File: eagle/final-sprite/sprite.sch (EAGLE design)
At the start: 62 parts, among them P1 SPRITE_PIN, P2 SPRITE_PIN, U1 CC430F5137, U2 DRV8833CRTER, U3 DRV8833CRTER, X1 TCXO_7Z

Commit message: Add review comments
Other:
- note added: "16 V"
- note added: "Eliminate pull-up"
- note added: "No interrupts? What's Data ENable?"
- note added: "Not connected... remove?"
- note added: "Regulated voltage output 1.5 (see Table 7)"
- note added: "Top row connectivity seems incorrect... Should be voltage dividers"
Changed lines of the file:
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@@
 <text x="-12.7" y="-264.16" size="1.778" layer="91">FIRMWARE:
 Pull-up required on NFAULT</text>
+<text x="182.88" y="-78.74" size="1.778" layer="91">Regulated voltage output 1.5
+(see Table 7)</text>
+<text x="182.88" y="-142.24" size="1.778" layer="91">Top row connectivity seems incorrect...
+Should be voltage dividers</text>
+<text x="91.44" y="-132.08" size="1.778" layer="91">Not connected... remove?</text>
+<text x="-17.78" y="-104.14" size="1.778" layer="91">16 V</text>
+<text x="48.26" y="-88.9" size="1.778" layer="91">Eliminate pull-up</text>
+<text x="27.94" y="-116.84" size="1.778" layer="91">No interrupts?
+What's Data ENable?</text>
 </plain>
 <instances>

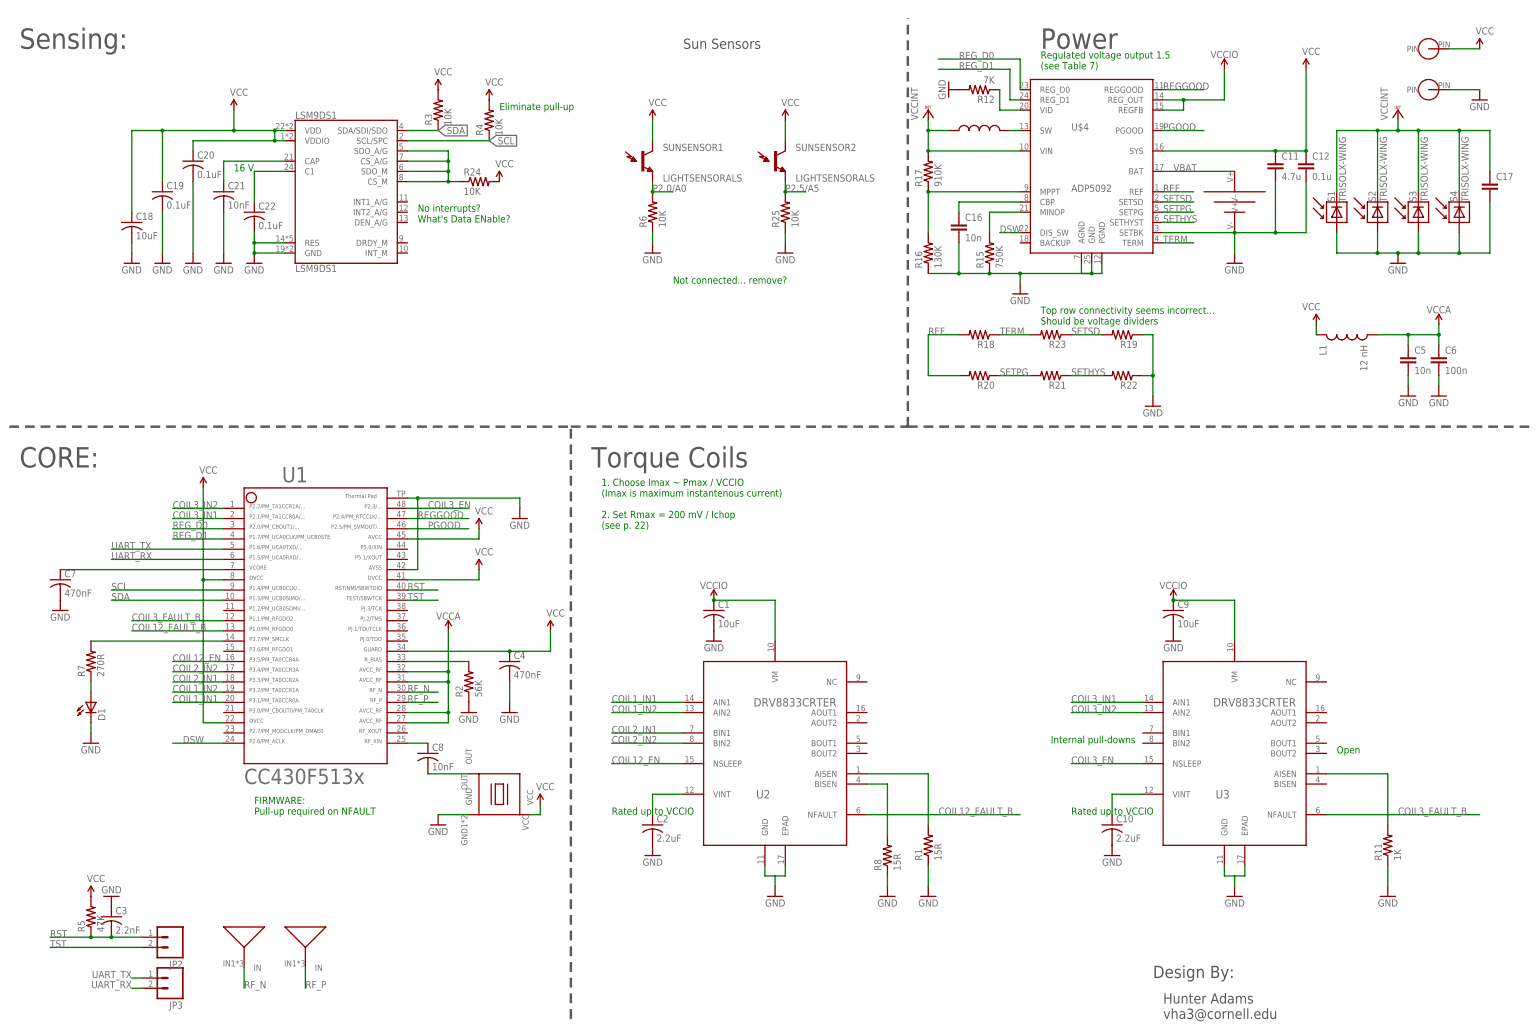
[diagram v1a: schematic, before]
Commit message: consistent board, pre-renumbering passives
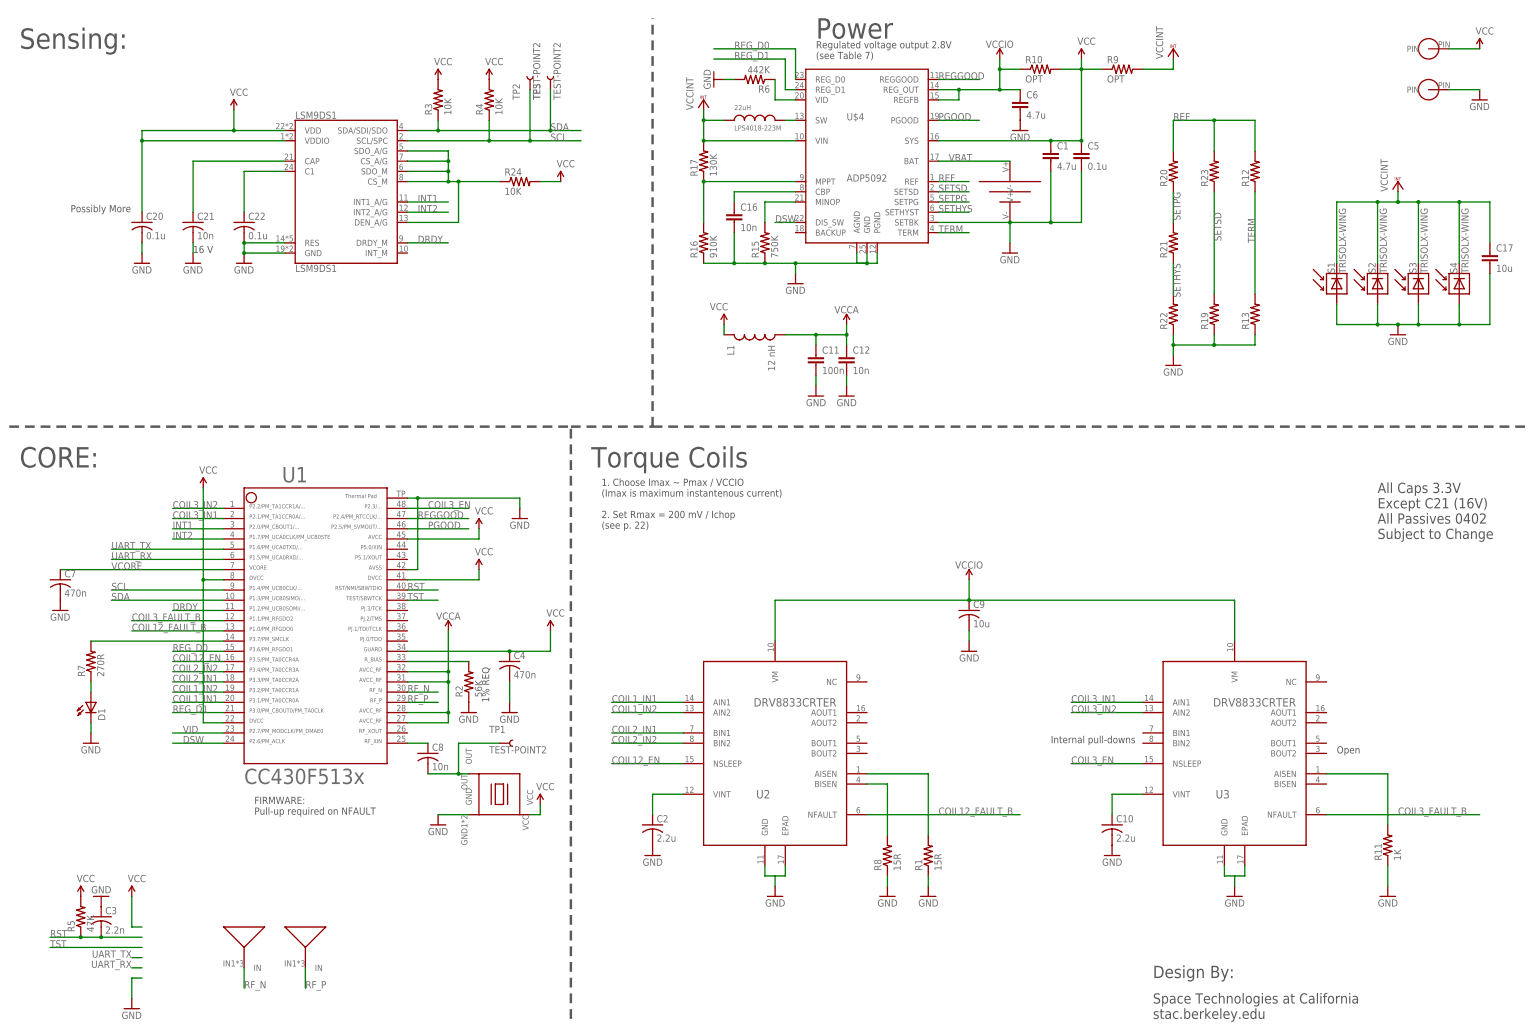
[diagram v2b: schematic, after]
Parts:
- removed C18: 10uF, rcl:C-USC0402
- removed C19: 0.1uF, rcl:C-USC0402
- removed JP2, JP3: (no value), SparkFun:M02PTH
- removed R18: (no value), resistor:R-US_R0402
- removed R25: 10K, rcl:R-US_R0402
- removed SUNSENSOR1, SUNSENSOR2: LIGHTSENSORALS, SparkFun-Sensors:LIGHTSENSORALS
- added R10, R9: OPT, resistor:R-US_R0402
- added R13: (no value), resistor:R-US_R0402
- added TP1, TP2, TP3: TEST-POINT2, SparkFun-Connectors:TEST-POINT2
- C1: value 10uF -> 4.7u; device rcl:C-USC0402 -> resistor:C-EUC0402
- C10, C2: value 2.2uF -> 2.2u
- C11: value 4.7u -> 100n
- C12: value 0.1u -> 10n
- C17: value (none) -> 10u
- C20, C22: value 0.1uF -> 0.1u
- C21, C8: value 10nF -> 10n
- C3: value 2.2nF -> 2.2n
- C4, C7: value 470nF -> 470n
- C5: value 10n -> 0.1u
- C6: value 100n -> 4.7u
- C9: value 10uF -> 10u
- R12: value 7K -> (none)
- R16: value 130K -> 910K
- R17: value 910K -> 130K
- R6: value 10K -> 442K; device rcl:R-US_R0402 -> resistor:R-US_R0402
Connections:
- net N$4 renamed VCORE
- removed net P2.0/A0: R6.2, SUNSENSOR1.E1
- removed net P2.5/A5: R25.2, SUNSENSOR2.E1
- new net DRDY: LSM9DS1.DRDY_M, U1.11
- new net INT1: LSM9DS1.INT1_A/G, U1.3
- new net INT2: LSM9DS1.INT2_A/G, U1.4
- new net VID: U1.23
- net GND: now also R13.1, R6.2; no longer C18.2, C19.2, R12.2, R25.1, R6.1
- net N$12: now also TP1.1
- net N$16: now also R6.1; no longer R12.1
- net N$7: now also LSM9DS1.DEN_A/G
- net REF: now also R12.2, R23.2; no longer R18.2
- net REG_D0: now also U1.15; no longer U1.3
- net REG_D1: now also U1.21; no longer U1.4
- net RST: no longer JP2.1
- net SCL: now also TP2.1
- net SDA: now also TP3.1
- net TERM: now also R12.1, R13.2; no longer R18.1, R23.2
- net TST: no longer JP2.2
- net UART_RX: no longer JP3.2
- net UART_TX: no longer JP3.1
- net VCC: now also C1.1, C5.1, R10.2, R9.1; no longer C11.1, C12.1, C18.1, C19.1, SUNSENSOR1.C1, SUNSENSOR2.C1
- net VCCA: now also C11.1, C12.1; no longer C5.1, C6.1
- net VCCINT: now also R9.2
- net VCCIO: now also C6.1, R10.1; no longer C1.1
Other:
- note added: "1% REQ"
- note added: "All Caps 3.3V Except C21 (16V) All Passives 0402 Subject to Change"
- note added: "Possibly More"
- note added: "Regulated voltage output 2.8V (see Table 7)"
- note added: "Space Technologies at California stac.berkeley.edu"
- note removed: "Eliminate pull-up"
- note removed: "Hunter Adams vha3@cornell.edu"
- note removed: "No interrupts? What's Data ENable?"
- note removed: "Not connected... remove?"
- note removed: "Rated up to VCCIO"
- note removed: "Regulated voltage output 1.5 (see Table 7)"
- note removed: "Sun Sensors"
- note removed: "Top row connectivity seems incorrect... Should be voltage dividers"
- moved on the sheet: C1, C11, C12, C16, C17, C20, C21, C22, C3, C5, C6, C9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
